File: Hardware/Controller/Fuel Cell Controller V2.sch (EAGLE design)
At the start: 130 parts, among them IC1 4081D, M1 MOSFETBOARD, T1 TEENSY_3.1_ALL_PINS, U1 SN74ALS153D, U2 MAX3221CPWR, U3 ATMEGA328P_TQFP, U4 ATMEGA328P_TQFP, U5 MAX3221CPWR, U6 ATMEGA328P_TQFP

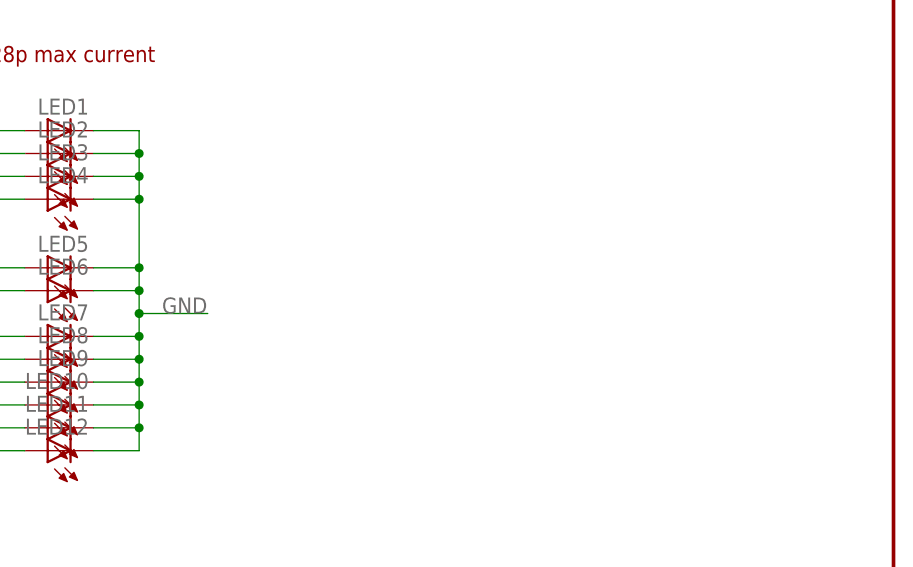
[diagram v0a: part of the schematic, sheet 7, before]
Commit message: some pin definitions
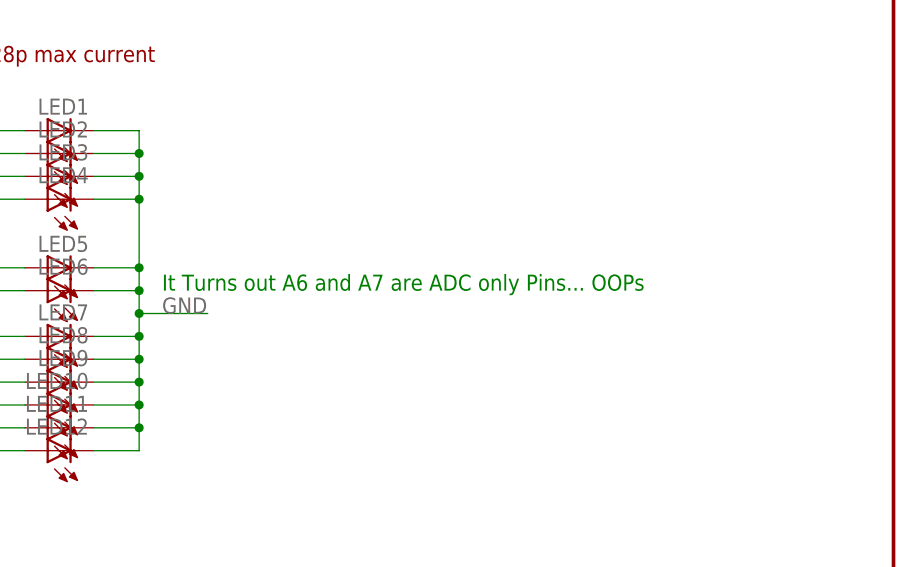
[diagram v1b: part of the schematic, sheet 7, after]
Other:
- note added: "It Turns out A6 and A7 are ADC only Pins... OOPs"
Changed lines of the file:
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@@
 <text x="91.44" y="170.18" size="6.4516" layer="94">STATUS LEDs</text>
 <text x="124.46" y="127" size="1.778" layer="94">Note: Check Atmega328p max current</text>
+<text x="167.64" y="101.6" size="1.778" layer="91">It Turns out A6 and A7 are ADC only Pins... OOPs</text>
 </plain>
 <instances>
